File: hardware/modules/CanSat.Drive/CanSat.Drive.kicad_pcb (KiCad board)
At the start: 2 copper layers, 60 x 40 mm, 66 parts, among them J101 Conn_01x02_Pin, J102 Conn_01x02_Pin, J301 Conn_01x04_MountingPin, J401 Conn_01x04_MountingPin, J501 Conn_01x02_Pin, J502 Conn_01x02_Pin, Q101 Q_NMOS_DGS, SW201 RESET_sw, SW601 Power Switch, U201 TPS3820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

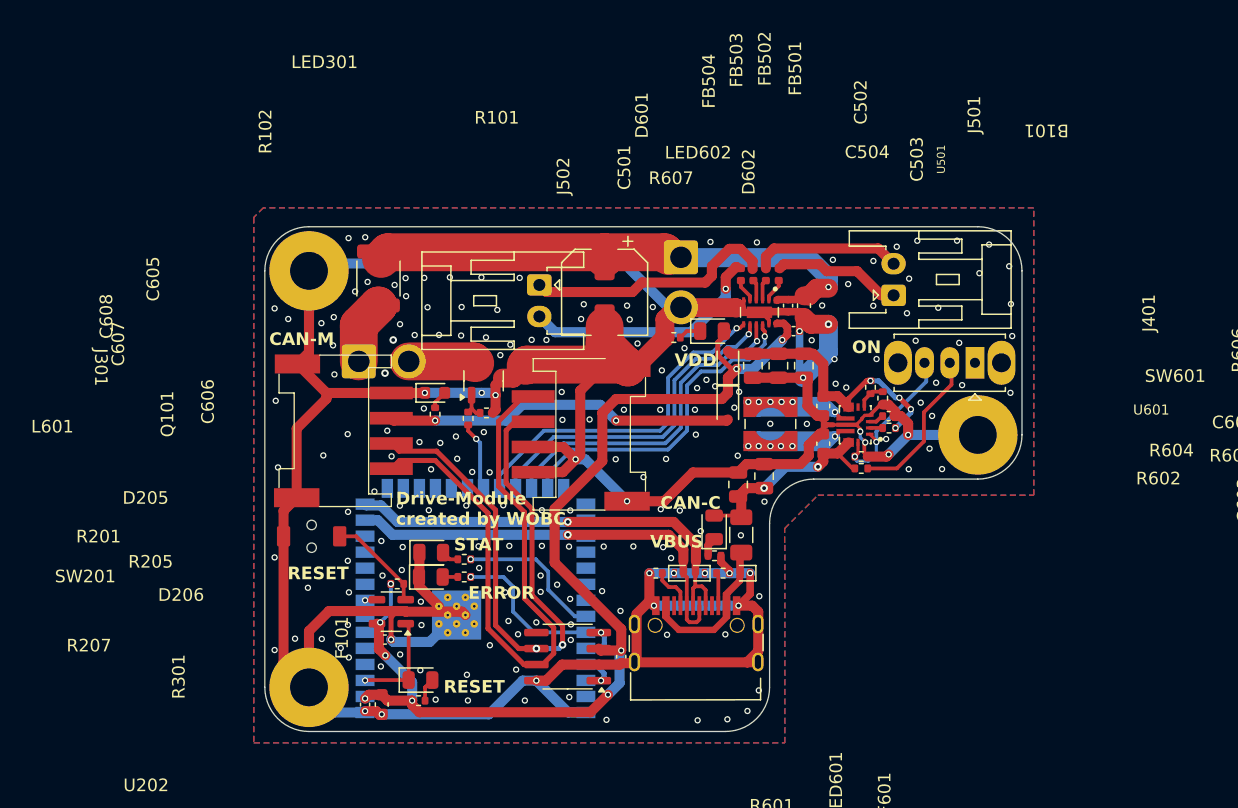
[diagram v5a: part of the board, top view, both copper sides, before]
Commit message: コネクタのの位置修正，LCSC番号間違い修正
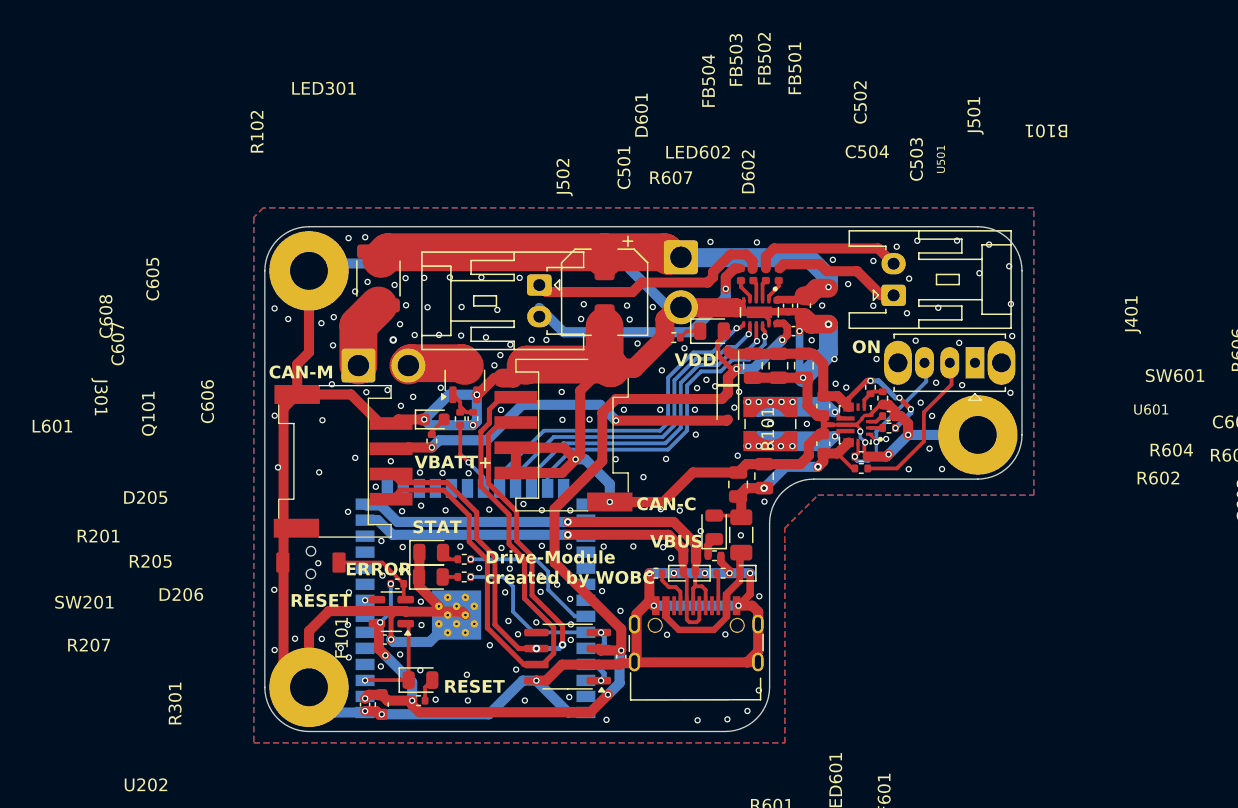
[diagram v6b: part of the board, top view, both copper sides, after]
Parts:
- moved J301 2.42 mm to (120.9, 89.4)
- moved R301 2.15 mm to (127.9, 87.8)
- moved LED301 2.11 mm to (128.0, 86.0)
- moved SW201 2.08 mm to (118.3, 97.4)
- moved Q101 1.48 mm to (130.5, 83.0)
- moved J401 1.37 mm to (138.2, 87.3)
- moved R101 1.16 mm to (131.1, 86.0), turned to -90 degrees
- moved R102 0.63 mm to (130.1, 86.0)
- moved J102 0.33 mm to (122.0, 81.8)
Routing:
- net GND: track 312.5 -> 323.2 mm, vias 198 -> 200
- net /CANL: track 47.0 -> 45.5 mm
- net /CANH: track 49.3 -> 48.2 mm
- net VBATT+: track 27.8 -> 28.7 mm
- net Net-(U201-MR): track 7.95 -> 7.14 mm
- net Net-(J102-Pin_2): track 5.33 -> 4.65 mm
- net Net-(Q101-G): track 2.26 -> 2.83 mm
- net Net-(J502-Pin_1): track 20.0 -> 19.4 mm
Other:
- board text added: "VBATT+"

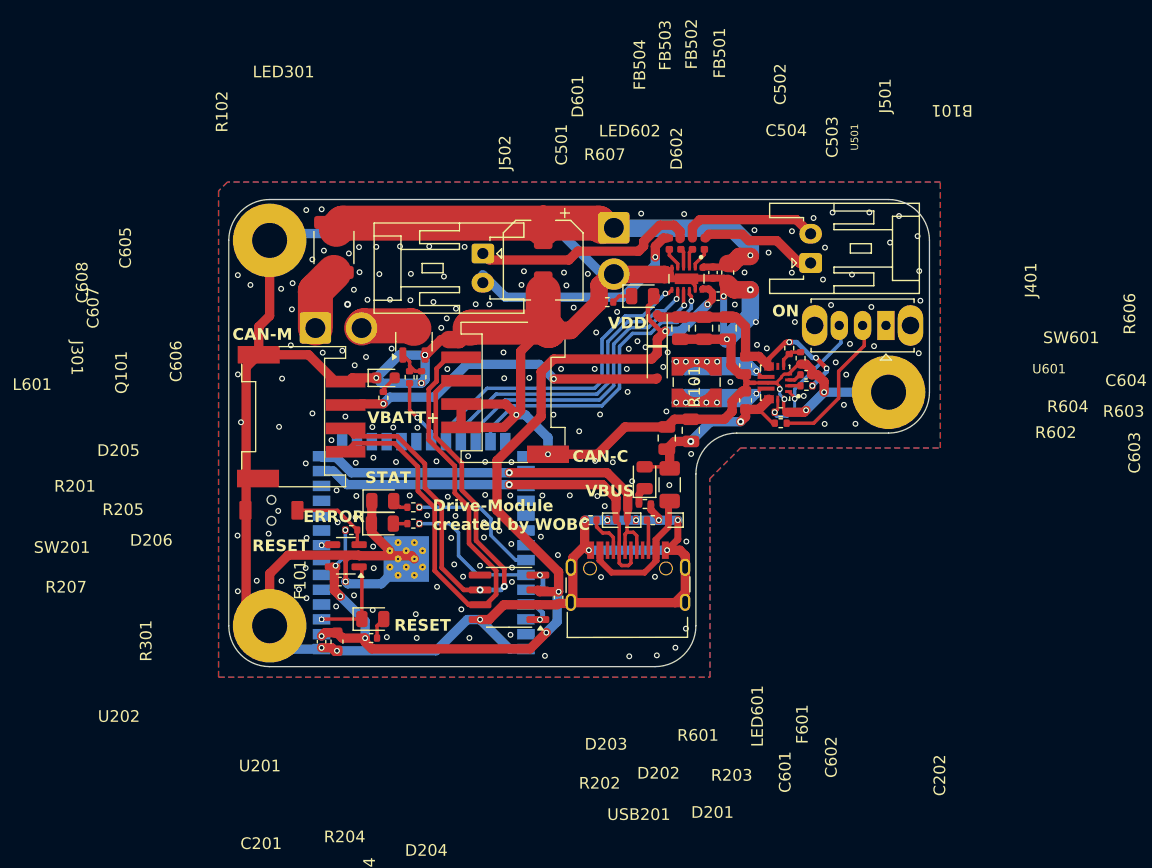
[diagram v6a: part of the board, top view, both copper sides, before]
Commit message: Groveコネクタ前もう少しスペース広げる．寸法的にギリギリ入るかどうかのライン
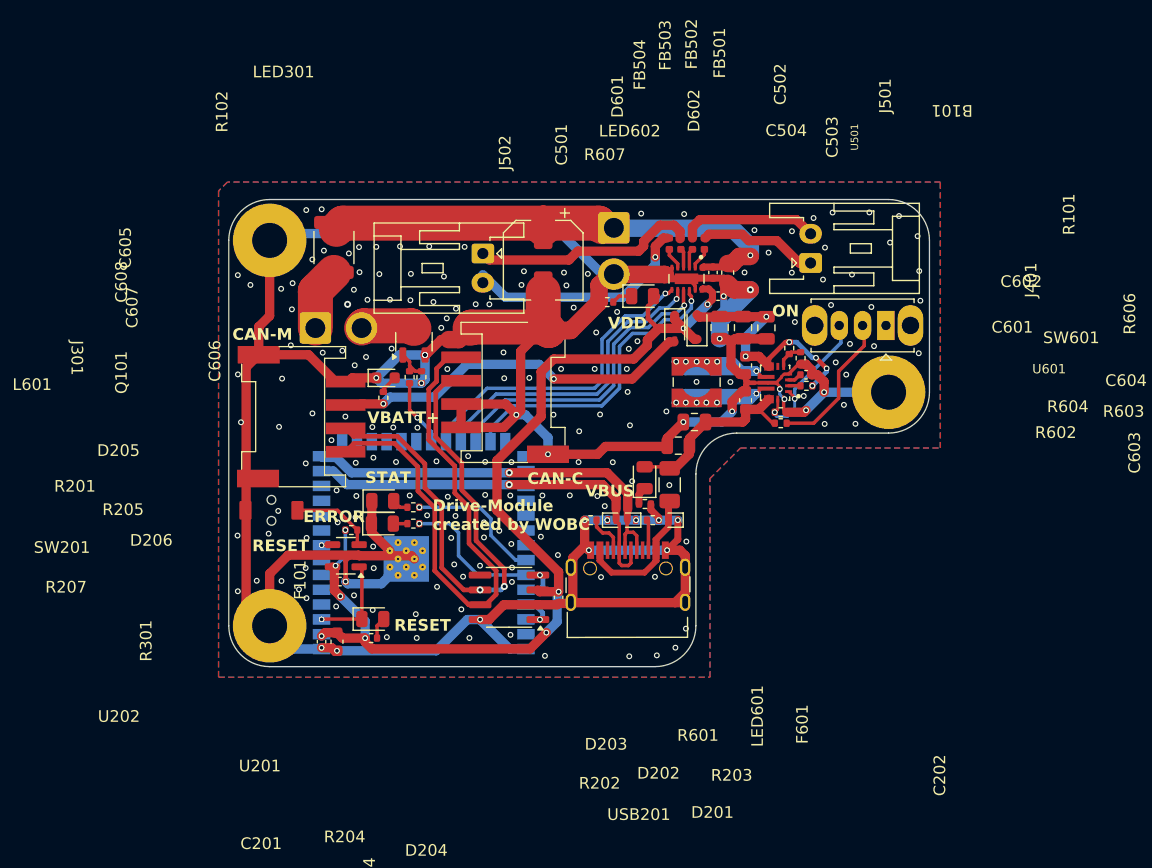
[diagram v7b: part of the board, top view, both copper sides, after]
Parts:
- moved D602 3.58 mm to (152.8, 81.7)
- moved D601 3.40 mm to (154.7, 81.7)
- moved C608 3.36 mm to (156.7, 81.7)
- moved C607 3.34 mm to (158.7, 81.8)
- moved C606 3.32 mm to (160.7, 81.8)
- moved C601 1.18 mm to (153.1, 91.8), turned to 180 degrees
- moved C602 0.77 mm to (154.5, 89.8), turned to 180 degrees
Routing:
- net VDD: track 84.5 -> 88.5 mm
- net VBATT+: track 28.7 -> 31.4 mm
- net Net-(LED601-A): track 16.7 -> 16.3 mm, vias 2 -> 0
- net Net-(D601-A2): track 22.0 -> 22.3 mm, vias 4 -> 6
- net GND: track 323.2 -> 323.4 mm, vias 200 -> 195
